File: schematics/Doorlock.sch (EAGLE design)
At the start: 44 parts, among them IC1 AT90S2313S, J1 RJ45, K1 G5V1, K2 G5V1, X1 RASPI_BOARD_B+#_H, X2 RIA182-04, X4 RIA182-05

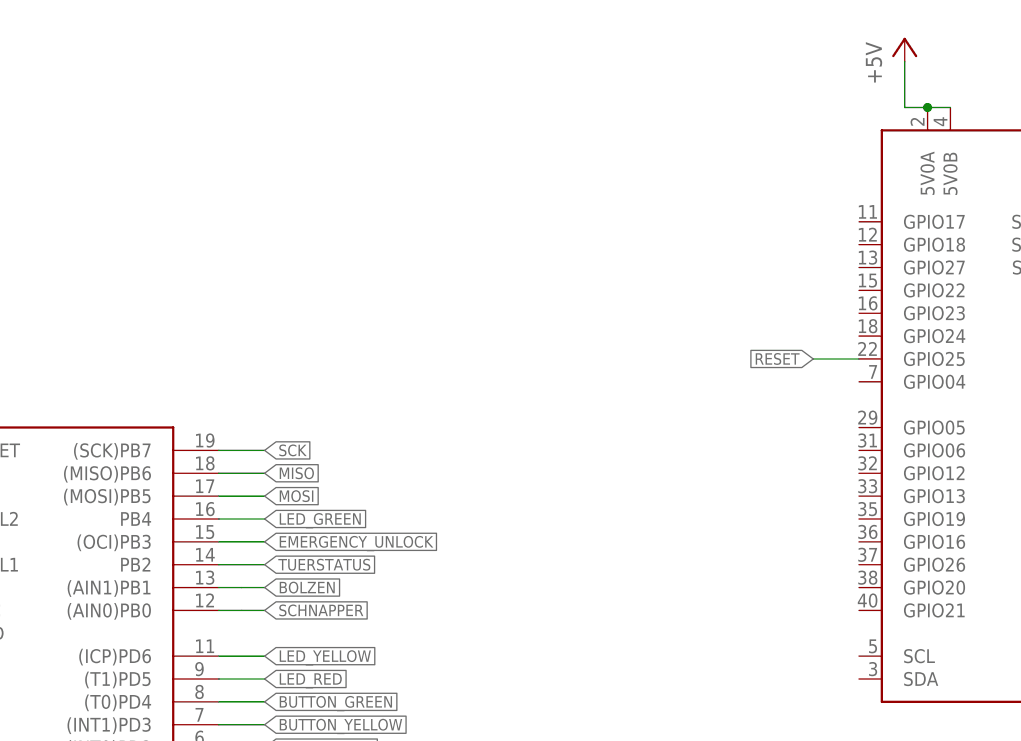
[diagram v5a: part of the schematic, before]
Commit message: schematics: add door state jumper
Signed-off-by: Ralf Ramsauer <ralf@binary-kitchen.de>
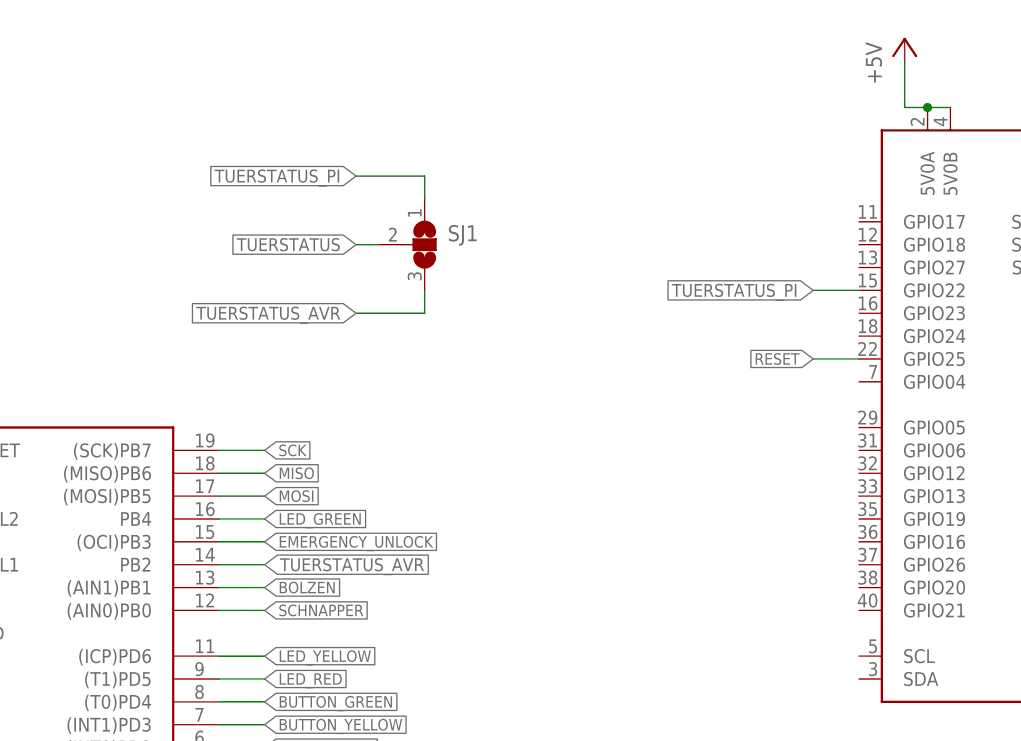
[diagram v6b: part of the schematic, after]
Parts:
- added SJ1: (no value), jumper:SJ2W
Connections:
- new net TUERSTATUS_AVR: IC1.PB2, SJ1.3
- new net TUERSTATUS_PI: SJ1.1, X1.GPIO22
- net TUERSTATUS: now also SJ1.2; no longer IC1.PB2
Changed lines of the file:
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@@
 <part name="R18" library="rcl" deviceset="R-EU_" device="R0805" value="1k"/>
 <part name="R19" library="rcl" deviceset="R-EU_" device="R0805" value="1k"/>
+<part name="SJ1" library="jumper" library_urn="urn:adsk.eagle:library:252" deviceset="SJ2W" device="" package3d_urn="urn:adsk.eagle:package:15474/1"/>
 </parts>
 <sheets>
@@
 <instance part="R18" gate="G$1" x="88.9" y="68.58"/>
 <instance part="R19" gate="G$1" x="88.9" y="83.82"/>
+<instance part="SJ1" gate="G$1" x="180.34" y="187.96"/>
 </instances>
 <busses>
@@
 </segment>
 <segment>
-<pinref part="IC1" gate="G$1" pin="PB2"/>
-<wire x1="157.48" y1="152.4" x2="162.56" y2="152.4" width="0.1524" layer="91"/>
-<label x="162.56" y="152.4" size="1.27" layer="95" font="fixed" xref="yes"/>
+<wire x1="175.26" y1="187.96" x2="172.72" y2="187.96" width="0.1524" layer="91"/>
+<label x="172.72" y="187.96" size="1.4224" layer="95" font="fixed" rot="R180" xref="yes"/>
+<pinref part="SJ1" gate="G$1" pin="2"/>
 </segment>
 </net>
@@
 </segment>
 </net>
+<net name="TUERSTATUS_AVR" class="0">
+<segment>
+<pinref part="SJ1" gate="G$1" pin="3"/>
+<wire x1="180.34" y1="182.88" x2="180.34" y2="180.34" width="0.1524" layer="91"/>
+<wire x1="180.34" y1="180.34" x2="172.72" y2="180.34" width="0.1524" layer="91"/>
+<label x="172.72" y="180.34" size="1.4224" layer="95" font="fixed" rot="R180" xref="yes"/>
+</segment>
+<segment>
+<pinref part="IC1" gate="G$1" pin="PB2"/>
+<wire x1="157.48" y1="152.4" x2="162.56" y2="152.4" width="0.1524" layer="91"/>
+<label x="162.56" y="152.4" size="1.4224" layer="95" font="fixed" xref="yes"/>
+</segment>
+</net>
+<net name="TUERSTATUS_PI" class="0">
+<segment>
+<pinref part="SJ1" gate="G$1" pin="1"/>
+<wire x1="180.34" y1="193.04" x2="180.34" y2="195.58" width="0.1524" layer="91"/>
+<wire x1="180.34" y1="195.58" x2="172.72" y2="195.58" width="0.1524" layer="91"/>
+<label x="172.72" y="195.58" size="1.4224" layer="95" font="fixed" rot="R180" xref="yes"/>
+</segment>
+<segment>
+<pinref part="X1" gate="G$1" pin="GPIO22"/>
+<wire x1="228.6" y1="182.88" x2="223.52" y2="182.88" width="0.1524" layer="91"/>
+<label x="223.52" y="182.88" size="1.4224" layer="95" font="fixed" rot="R180" xref="yes"/>
+</segment>
+</net>

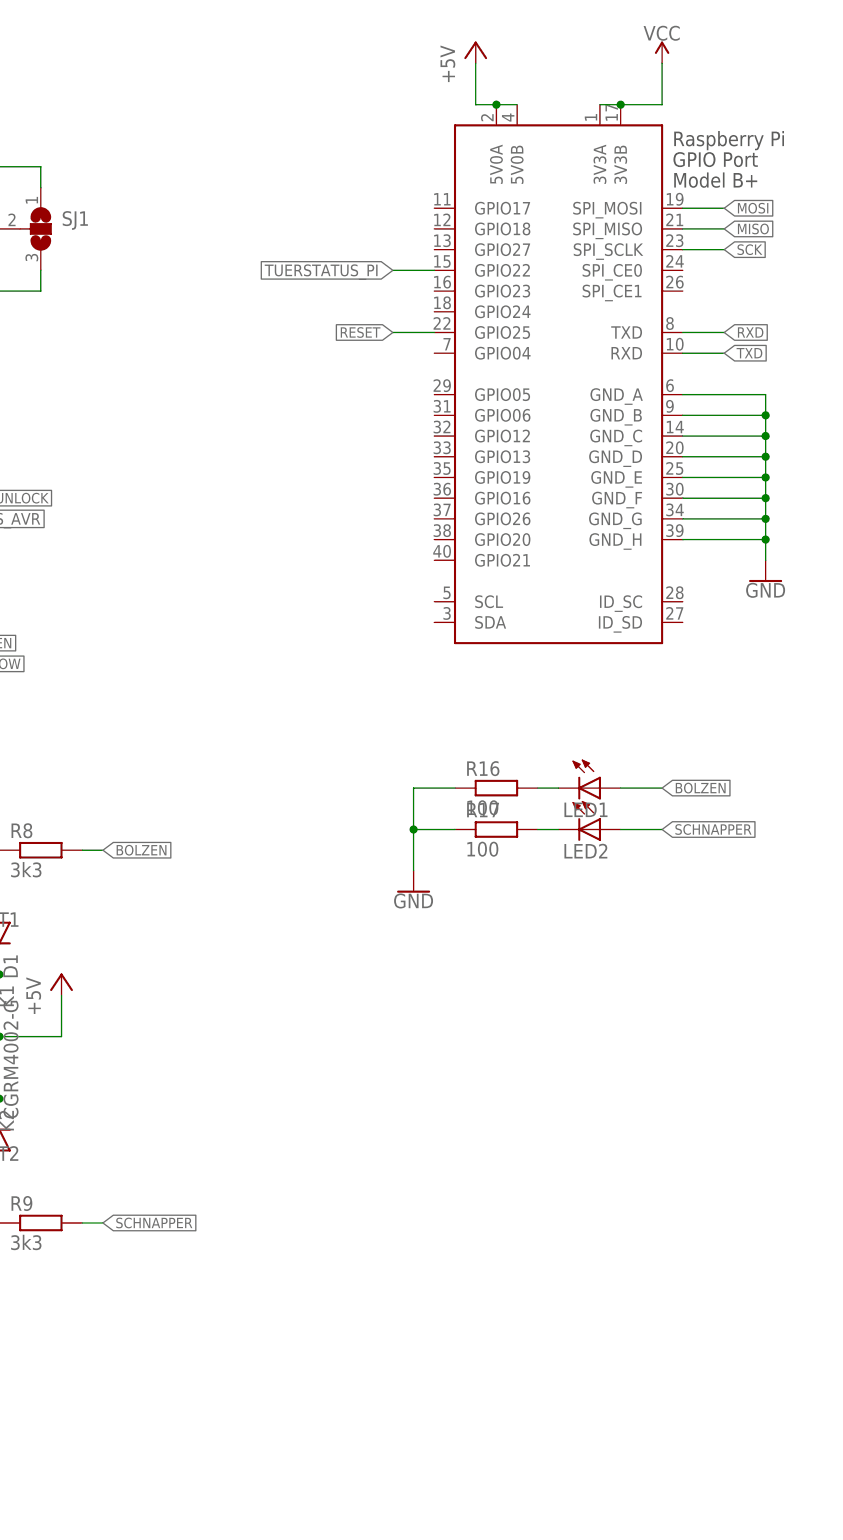
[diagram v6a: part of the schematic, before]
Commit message: schematics: add Raspberry Pi Hat EEPROM
Signed-off-by: Ralf Ramsauer <ralf@binary-kitchen.de>
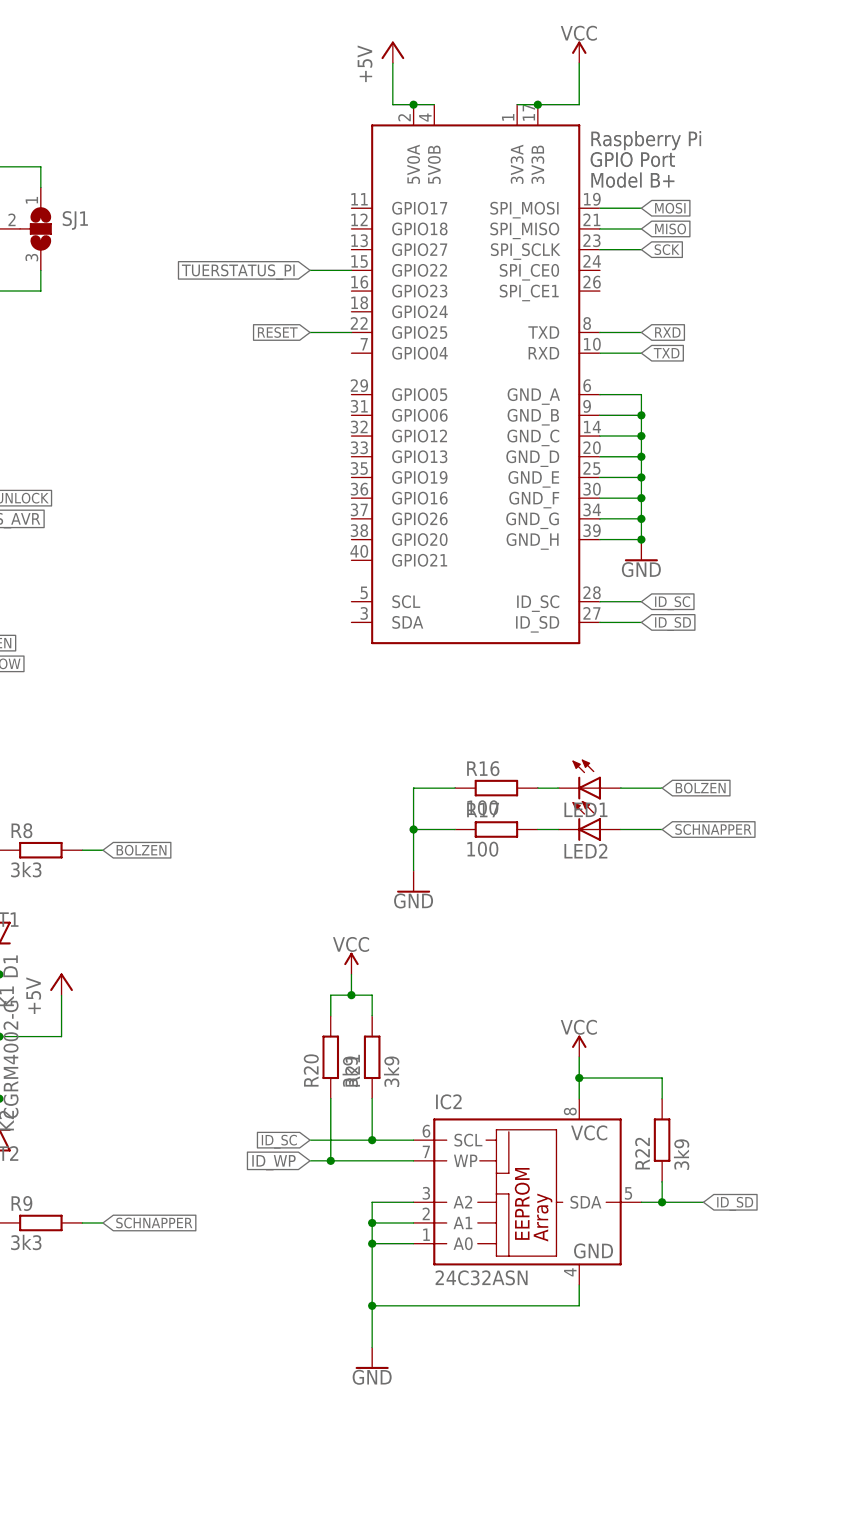
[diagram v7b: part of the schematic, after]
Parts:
- added IC2: 24C32ASN, microchip:24C32ASN
- added R20, R21, R22: 3k9, rcl:R-EU_R0805
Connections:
- new net ID_SC: IC2.SCL, R21.1, X1.ID_SC
- new net ID_SD: IC2.SDA, R22.1, X1.ID_SD
- new net ID_WP: IC2.WP, R20.1
- net GND: now also IC2.A0, IC2.A1, IC2.A2, IC2.GND
- net VCC: now also IC2.VCC, R20.2, R21.2, R22.2
